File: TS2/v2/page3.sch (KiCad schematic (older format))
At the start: 7 parts, among them K1 74LS260, K2 74LS260, K3 74LS138, K4 25LS2548

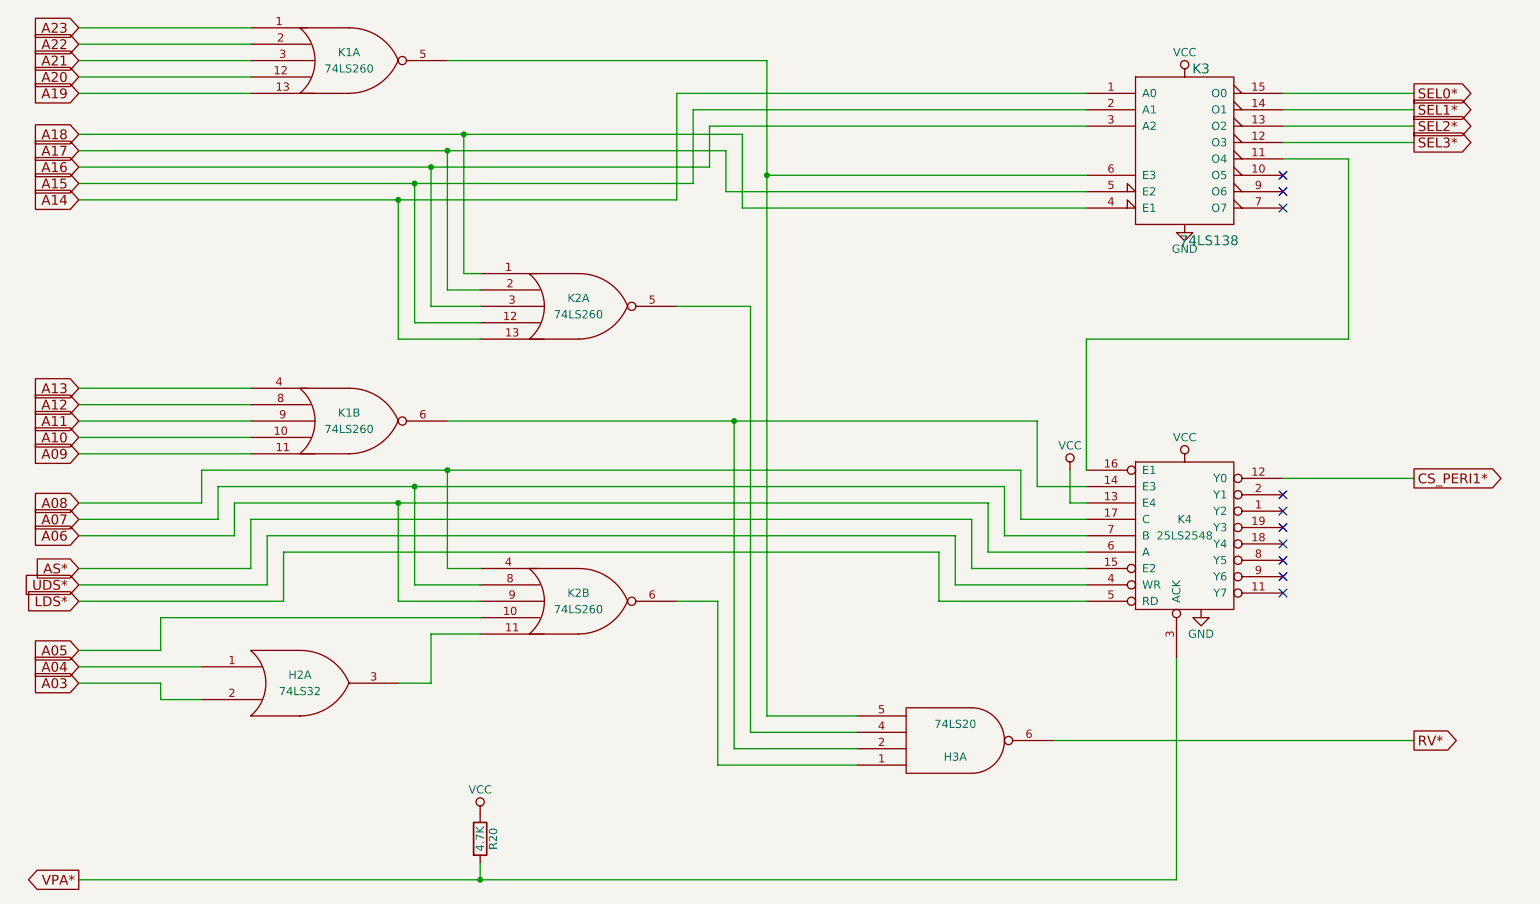
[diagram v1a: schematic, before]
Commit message: more fixup of deleted pages.
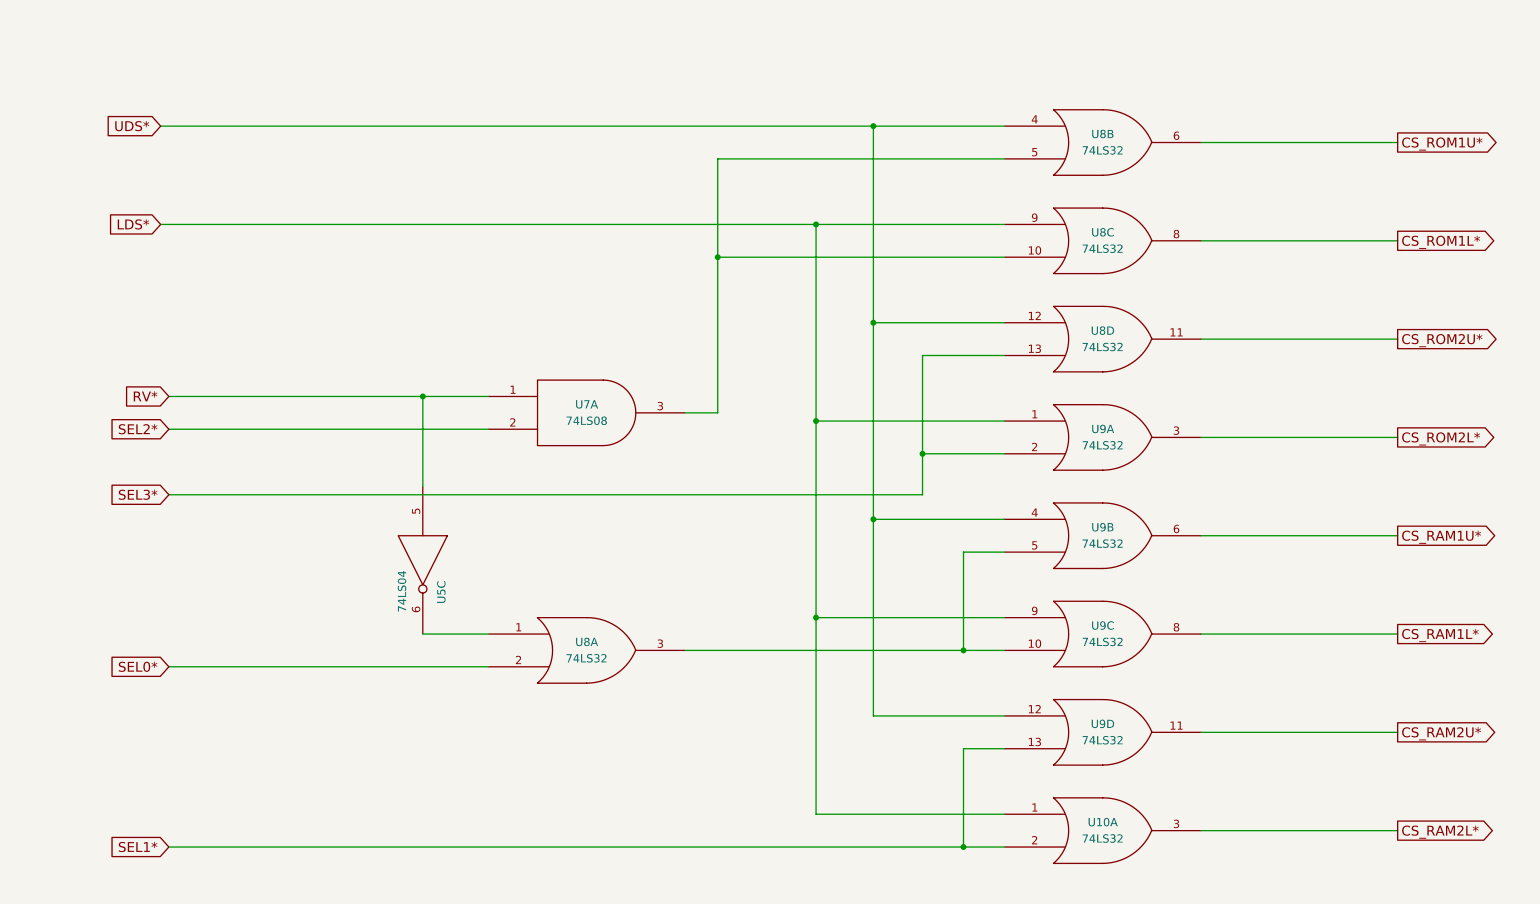
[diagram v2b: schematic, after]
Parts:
- removed H2: 74LS32, symbol 74LS32
- removed H3: 74LS20, symbol 74LS20
- removed K1, K2: 74LS260, symbol 74LS260
- removed K3: 74LS138, ~, symbol 74LS138
- removed K4: 25LS2548, symbol 25LS2548
- removed R20: 4.7K, symbol R
- added U10, U8, U9: 74LS32, symbol 74LS32
- added U5: 74LS04, symbol 74LS04
- added U7: 74LS08, symbol 74LS08
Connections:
- net GND: now also U10.7 (GND), U5.7 (GND), U7.7 (GND), U8.7 (GND), U8.7 (GND), U8.7 (GND), U8.7 (GND), U9.7 (GND), U9.7 (GND), U9.7 (GND), U9.7 (GND)
- net LDS*: now also U10.1, U8.9, U9.1, U9.9
- net RV*: now also U5.5, U7.1
- net SEL0*: now also U8.2
- net SEL1*: now also U10.2, U9.13
- net SEL2*: now also U7.2
- net SEL3*: now also U8.13, U9.2
- net UDS*: now also U8.12, U8.4, U9.12, U9.4
- net VCC: now also U10.14 (VCC), U5.14 (VCC), U7.14 (VCC), U8.14 (VCC), U8.14 (VCC), U8.14 (VCC), U8.14 (VCC), U9.14 (VCC), U9.14 (VCC), U9.14 (VCC), U9.14 (VCC)
- new net: U7.3, U8.10, U8.5
- new net: U5.6, U8.1
- new net: U8.3, U9.10, U9.5
- new net CS_RAM1L*: U9.8
- new net CS_RAM1U*: U9.6
- new net CS_RAM2L*: U10.3
- new net CS_RAM2U*: U9.11
- new net CS_ROM1L*: U8.8
- new net CS_ROM1U*: U8.6
- new net CS_ROM2L*: U9.3
- new net CS_ROM2U*: U8.11
- no-connect marks 10 -> 0
